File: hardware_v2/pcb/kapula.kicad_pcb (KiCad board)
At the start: 4 copper layers, 50 x 59 mm, 166 parts, among them J1 Conn_02x10_Odd_Even, J2 Conn_02x10_Odd_Even, J3 U.FL, J4 U.FL, J5 U.FL, J6 U.FL, Q1 AO3401A, Q2 AO3400A, Q3 AO3400A, Q4 AO3400A, Q5 AO3401A, Q6 BSS84, T1 BW21S7511A01TF, T2 BW21S7511A01TF, T3 BW21S7511A01TF, T4 BW21S7511A01TF, U1 TP4054, U2 DW01+G, U3 XC6206P332MR, U4 FM8002A, U5 EFR32FG14P233F256GM48-B, U6 DSB221SDN, U7 XA213-G4J, Y1 32768 Hz

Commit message: PCB: Fix TCXO model in schematic
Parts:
- U6: value DSB221SDN -> TG2016SMN 38.4000M-MCGNNM3
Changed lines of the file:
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@@
         (effects (font (size 0.7 0.7) (thickness 0.15)))
     )
-    (fp_text value "DSB221SDN" (at 0 1 90 unlocked) (layer "F.Fab")
+    (fp_text value "TG2016SMN 38.4000M-MCGNNM3" (at 0 1 90 unlocked) (layer "F.Fab")
         (effects (font (size 1 1) (thickness 0.15)))
     )

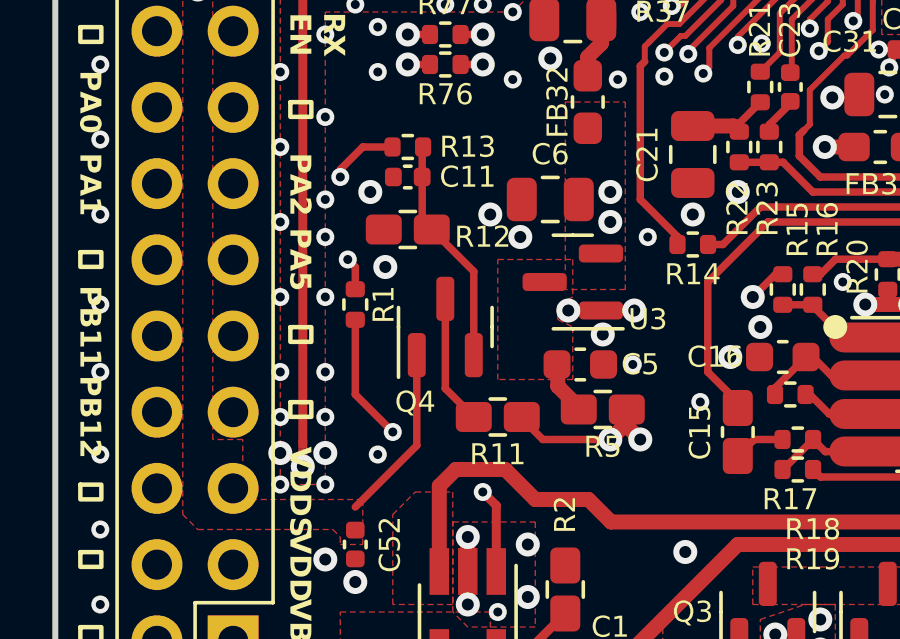
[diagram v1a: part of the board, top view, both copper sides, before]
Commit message: PCB: Add DVDD to expansion header
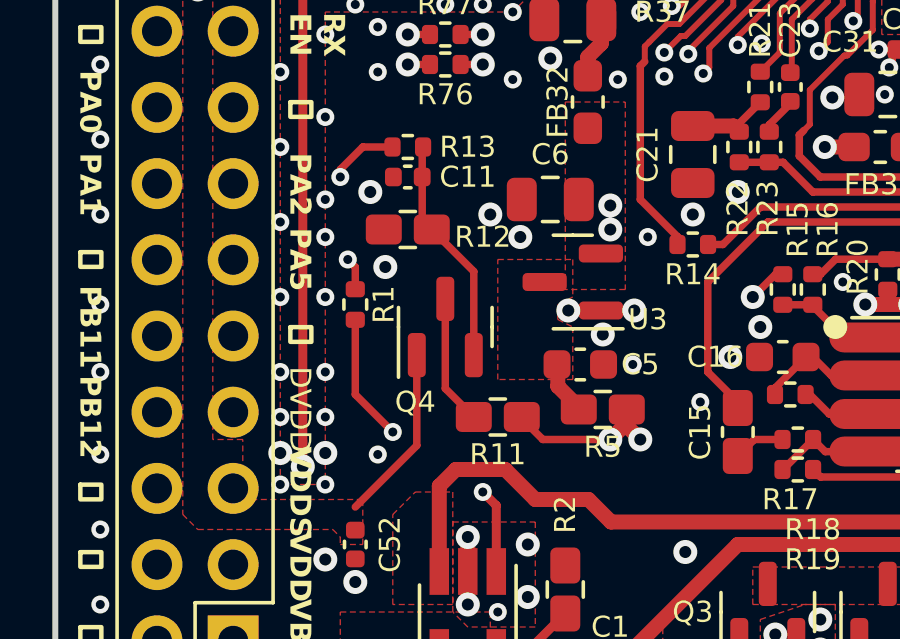
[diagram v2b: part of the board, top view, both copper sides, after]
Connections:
- J2 pad 7: GND -> /1V8
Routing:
- net /1V8: track 30.5 -> 65.0 mm
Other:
- board text added: "DVDD"

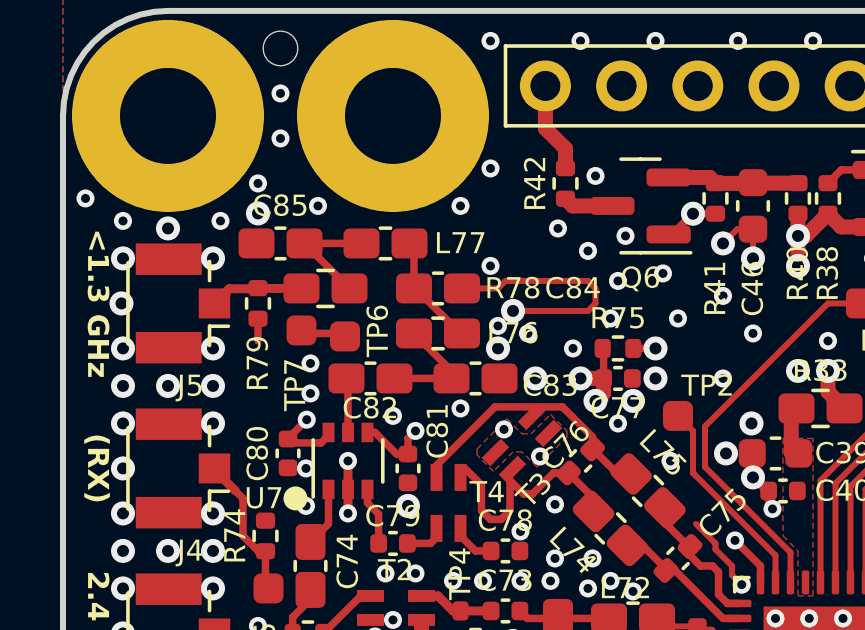
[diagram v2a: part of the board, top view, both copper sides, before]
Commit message: PCB: Optimize lowpass filter
* Reduce second harmonic stub length by 1 mm
  to move notch frequency closer to 870 MHz.
* Use footprints of correct size for capacitors and inductors.
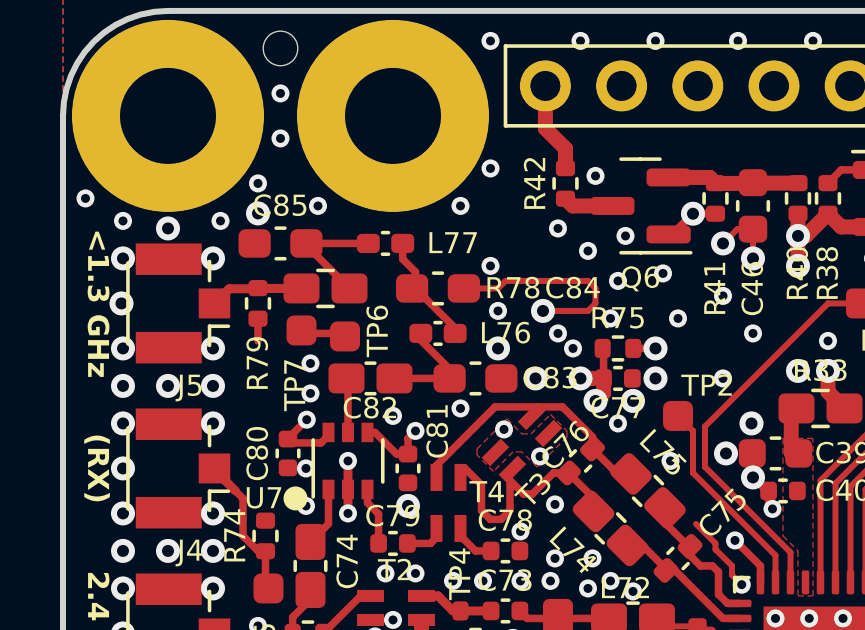
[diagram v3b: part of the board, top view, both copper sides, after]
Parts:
- C83, C84, C85: footprint kapula:C_0402_to_0603_HandSolder -> Capacitor_SMD:C_0603_1608Metric_Pad1.08x0.95mm_HandSolder
- L76, L77: footprint kapula:L_0402_to_0603_HandSolder -> Inductor_SMD:L_0402_1005Metric_Pad0.77x0.64mm_HandSolder
- moved NT72 1.00 mm to (116.5, 67.5)
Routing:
- net Net-(C84-Pad2): track 7.31 -> 6.31 mm

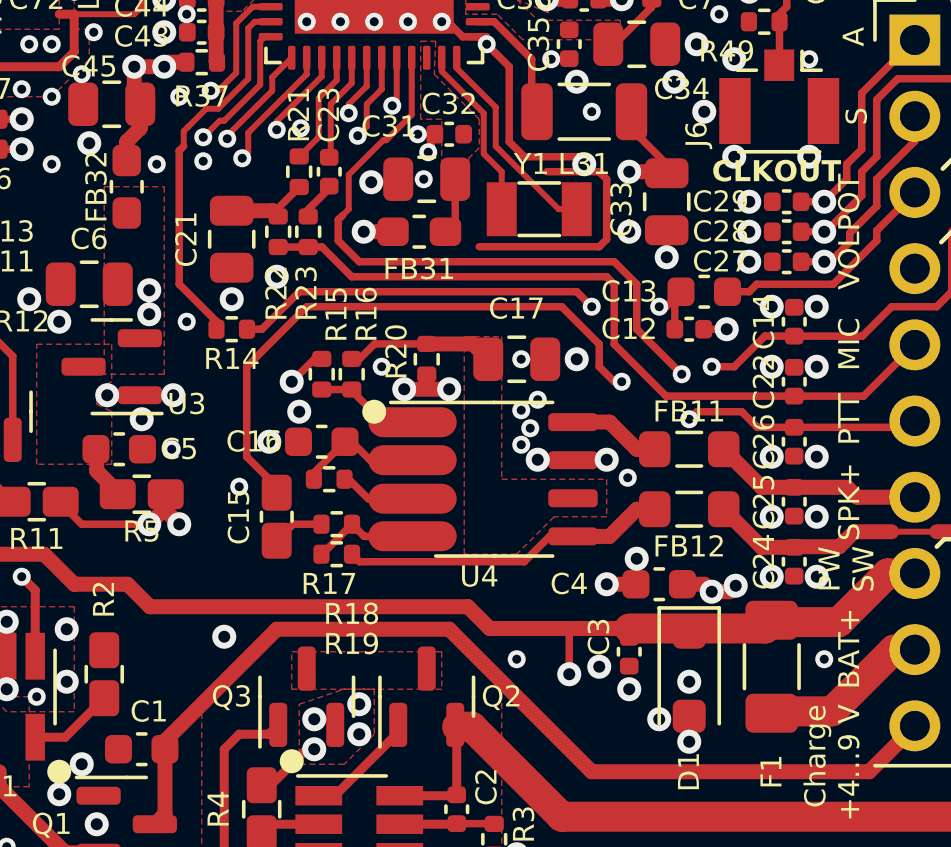
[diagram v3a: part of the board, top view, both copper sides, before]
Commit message: PCB: Changes to audio power amplifier circuit
* Increase maximum gain
* Change some footprint sizes
* Reduce shutdown pull-up resistor value
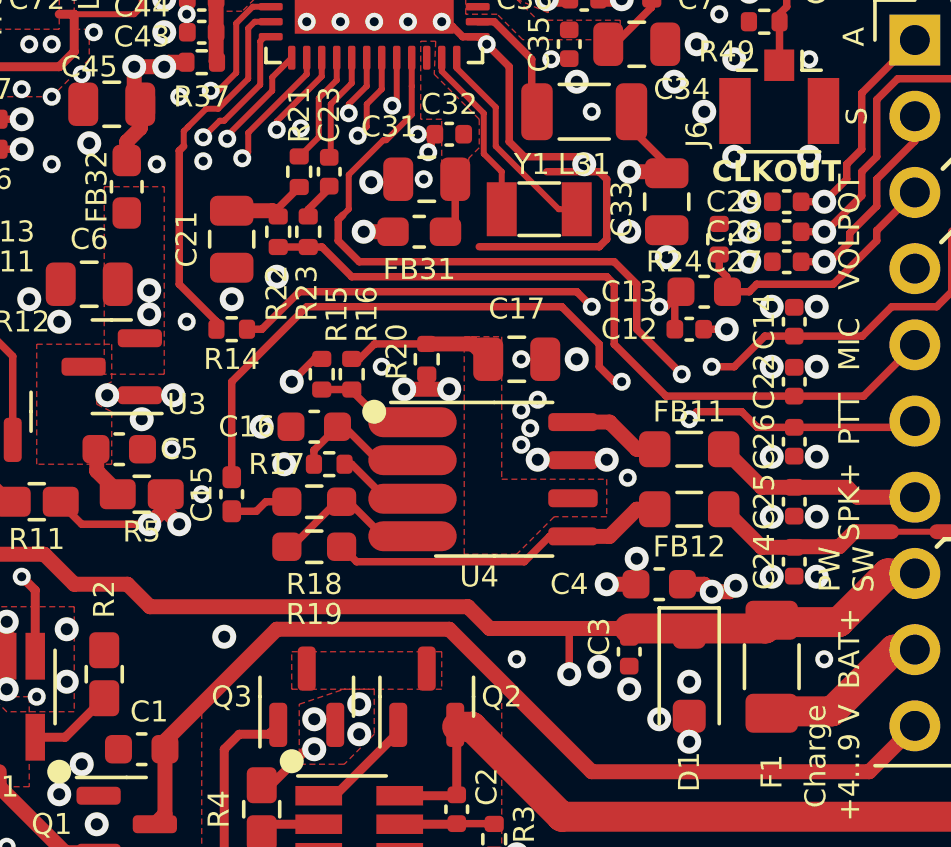
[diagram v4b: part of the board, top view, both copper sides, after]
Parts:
- added R24: 1M, Resistor_SMD:R_0402_1005Metric, F.Cu at (137.5, 89.5)
- C15: footprint kapula:C_0402_to_0603_HandSolder -> Capacitor_SMD:C_0402_1005Metric_Pad0.74x0.62mm_HandSolder
- R16: value 1M -> 330k
- R18: footprint Resistor_SMD:R_0402_1005Metric -> Resistor_SMD:R_0603_1608Metric_Pad0.98x0.95mm_HandSolder
- R19: value 22k -> 47k; footprint Resistor_SMD:R_0402_1005Metric -> Resistor_SMD:R_0603_1608Metric_Pad0.98x0.95mm_HandSolder
- moved C15 1.68 mm to (121.2, 98.0)
- moved R18 1.06 mm to (124.0, 98.2)
- moved R19 0.79 mm to (124.0, 99.8)
- moved C16 0.56 mm to (124.0, 95.8)
- moved R17 0.50 mm to (124.5, 97.0)
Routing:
- net /VOL_Out: track 7.82 -> 9.17 mm
- net /AMP+IN: track 3.51 -> 4.79 mm
- net /VOL_In: track 36.1 -> 35.1 mm
- net /AMP-IN: track 5.67 -> 6.26 mm

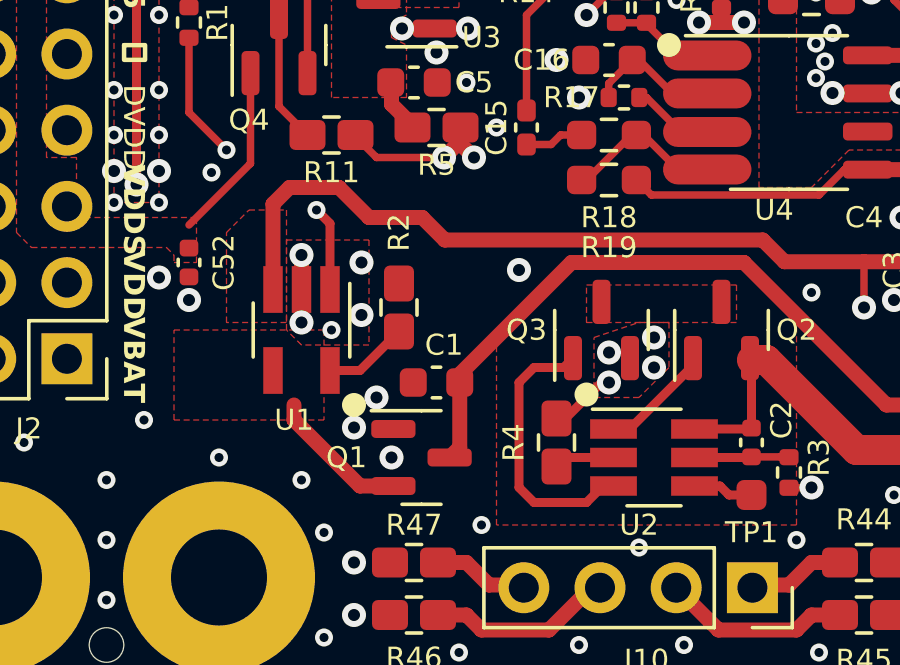
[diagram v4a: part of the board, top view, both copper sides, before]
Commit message: PCB: Improve battery charger cooling by adding zones for all pins
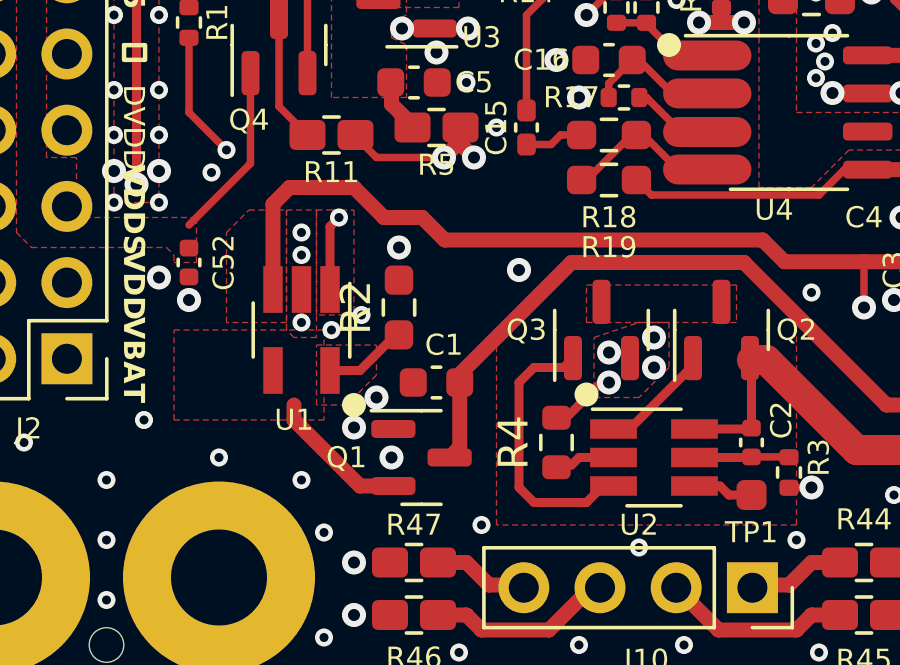
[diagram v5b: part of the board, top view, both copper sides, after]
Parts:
- R2: footprint kapula:R_0402_to_0603_HandSolder -> Resistor_SMD:R_0603_1608Metric_Pad0.98x0.95mm_HandSolder
- R4: footprint kapula:R_0402_to_0603_HandSolder -> Resistor_SMD:R_0603_1608Metric
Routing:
- net GND: track 65.4 -> 64.3 mm, vias 392 -> 393
- net /~{CHRG}: track 10.9 -> 11.5 mm
- added copper zone on F.Cu, net /BC_PROG
- added copper zone on F.Cu, net /~{CHRG}

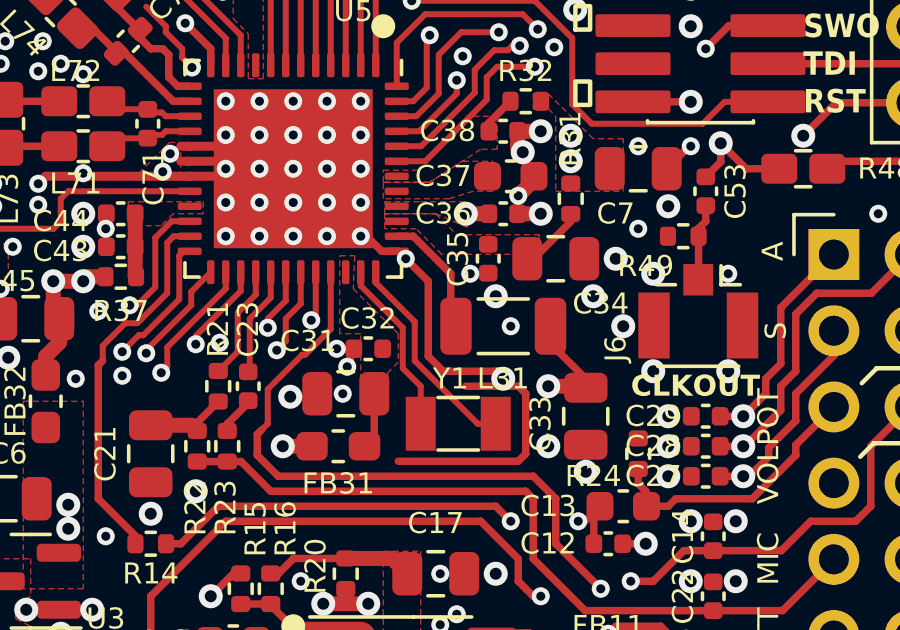
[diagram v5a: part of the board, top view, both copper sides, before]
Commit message: PCB: Move a via that was very close to EFR32 pad
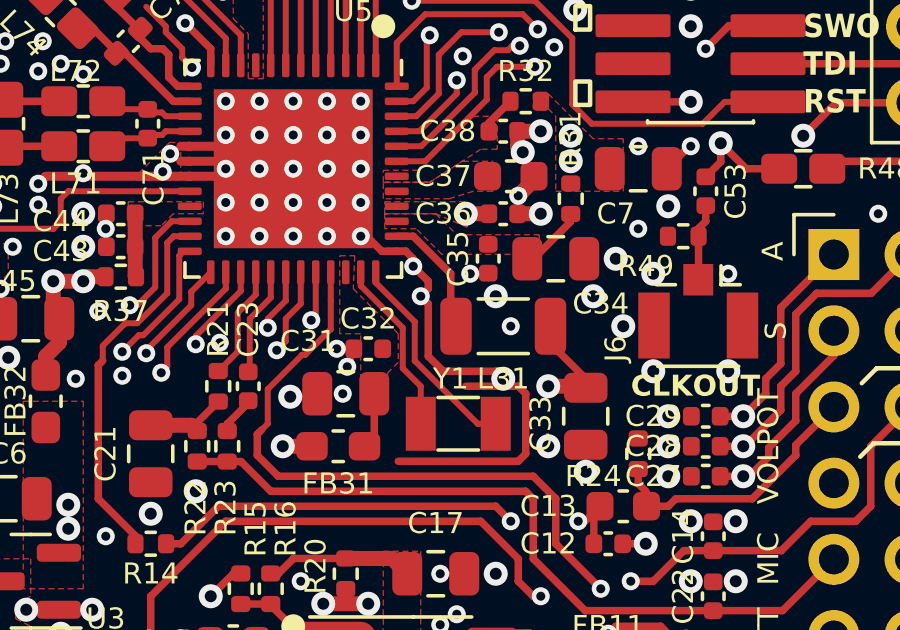
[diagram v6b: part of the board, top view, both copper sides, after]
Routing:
- net GND: track 64.3 -> 64.7 mm, vias 393 -> 394
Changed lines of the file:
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@@
   (segment (start 129.45 82.75) (end 128.95 82.75) (width 0.25) (layer "F.Cu") (net 2))
   (segment (start 128.399999 82.399999) (end 128 82) (width 0.25) (layer "F.Cu") (net 2))
+  (segment (start 130.25 84.25) (end 130.5 84.5) (width 0.25) (layer "F.Cu") (net 2))
+  (segment (start 130 83.25) (end 130.5 83.75) (width 0.25) (layer "F.Cu") (net 2))
   (segment (start 143 66.74) (end 142.51 66.74) (width 0.25) (layer "F.Cu") (net 2))
-  (segment (start 133 87) (end 132.75 86.75) (width 0.25) (layer "F.Cu") (net 2))
+  (segment (start 131 86.75) (end 132.75 86.75) (width 0.25) (layer "F.Cu") (net 2))
   (segment (start 133.5 87.25) (end 133.75 87.5) (width 0.25) (layer "F.Cu") (net 2))
+  (segment (start 129.75 82.75) (end 129.45 82.75) (width 0.25) (layer "F.Cu") (net 2))
   (segment (start 133.48 81.5) (end 134.25 81.5) (width 0.5) (layer "F.Cu") (net 2))
   (segment (start 121.75 75.45) (end 121.75 75.25) (width 0.2) (layer "F.Cu") (net 2))
@@
   (segment (start 117.750008 80.249992) (end 117.5 80.5) (width 0.3) (layer "F.Cu") (net 2))
   (segment (start 122.475 64.775) (end 122 65.25) (width 0.2) (layer "F.Cu") (net 2))
-  (segment (start 130.5 86.25) (end 130.5 83.75) (width 0.25) (layer "F.Cu") (net 2))
   (segment (start 133.5 80.9) (end 134.025 80.375) (width 0.5) (layer "F.Cu") (net 2))
-  (segment (start 131 86.75) (end 130.5 86.25) (width 0.25) (layer "F.Cu") (net 2))
-  (segment (start 129.5 82.75) (end 129.75 83) (width 0.25) (layer "F.Cu") (net 2))
+  (segment (start 130.5 84) (end 130.25 84.25) (width 0.25) (layer "F.Cu") (net 2))
   (segment (start 122.3 76.3) (end 122.3 76) (width 0.2) (layer "F.Cu") (net 2))
   (segment (start 123.75 106.5) (end 124 106.5) (width 0.3) (layer "F.Cu") (net 2))
+  (segment (start 130 83) (end 129.75 82.75) (width 0.25) (layer "F.Cu") (net 2))
   (segment (start 122.625 76.625) (end 122.5 76.5) (width 0.25) (layer "F.Cu") (net 2))
   (segment (start 121.75 75.25) (end 121.1 74.6) (width 0.2) (layer "F.Cu") (net 2))
   (segment (start 139 68.68) (end 139 69.25) (width 0.25) (layer "F.Cu") (net 2))
+  (segment (start 130.5 86.25) (end 131 86.75) (width 0.25) (layer "F.Cu") (net 2))
   (segment (start 139.2 79.25) (end 138.45 80) (width 0.25) (layer "F.Cu") (net 2))
   (segment (start 133.48 78.75) (end 134.25 78.75) (width 0.5) (layer "F.Cu") (net 2))
@@
   (segment (start 123.52 73.5) (end 123.52 73.97) (width 0.25) (layer "F.Cu") (net 2))
   (segment (start 122.625 76.625) (end 122.3 76.3) (width 0.2) (layer "F.Cu") (net 2))
+  (segment (start 130.5 84.5) (end 130.5 86.25) (width 0.25) (layer "F.Cu") (net 2))
+  (segment (start 130 83.25) (end 130 83) (width 0.25) (layer "F.Cu") (net 2))
   (segment (start 122.55 79.75) (end 122.25 79.75) (width 0.3) (layer "F.Cu") (net 2))
   (segment (start 109.5 73.45) (end 109.5 72.5) (width 0.3) (layer "F.Cu") (net 2))
-  (segment (start 132.75 86.75) (end 131 86.75) (width 0.25) (layer "F.Cu") (net 2))
   (segment (start 133.65 79.45) (end 133.48 79.28) (width 0.5) (layer "F.Cu") (net 2))
   (segment (start 142.51 66.74) (end 142.25 67) (width 0.25) (layer "F.Cu") (net 2))
@@
   (segment (start 127.45 86) (end 128.02 86) (width 0.25) (layer "F.Cu") (net 2))
   (segment (start 127.9 86.5) (end 127.8 86.6) (width 0.25) (layer "F.Cu") (net 2))
+  (segment (start 132.75 86.75) (end 133 87) (width 0.25) (layer "F.Cu") (net 2))
   (segment (start 122.25 107.7) (end 122.55 107.7) (width 0.3) (layer "F.Cu") (net 2))
   (segment (start 136.98 92.5) (end 137.75 92.5) (width 0.25) (layer "F.Cu") (net 2))
@@
   (segment (start 133.48 79.28) (end 133.48 78.75) (width 0.5) (layer "F.Cu") (net 2))
   (segment (start 134.025 80.375) (end 134.025 80.25) (width 0.5) (layer "F.Cu") (net 2))
-  (segment (start 129.45 82.75) (end 129.5 82.75) (width 0.25) (layer "F.Cu") (net 2))
   (segment (start 106.5 67.76) (end 106.5 68.5) (width 0.25) (layer "F.Cu") (net 2))
-  (segment (start 130.5 83.75) (end 129.75 83) (width 0.25) (layer "F.Cu") (net 2))
+  (segment (start 130.5 83.75) (end 130.5 84) (width 0.25) (layer "F.Cu") (net 2))
   (segment (start 133.75 89.5) (end 133.5 89.75) (width 0.25) (layer "F.Cu") (net 2))
   (segment (start 114.26 78.5) (end 115 78.5) (width 0.5) (layer "F.Cu") (net 2))
@@
   (via (at 141 103.5) (size 0.6) (drill 0.3) (layers "F.Cu" "B.Cu") (free) (net 2))
   (via (at 113 76.5) (size 0.6) (drill 0.3) (layers "F.Cu" "B.Cu") (free) (net 2))
+  (via (at 130.25 84.25) (size 0.6) (drill 0.3) (layers "F.Cu" "B.Cu") (net 2))
   (via (at 124 105.5) (size 0.8) (drill 0.4) (layers "F.Cu" "B.Cu") (free) (net 2))
   (via (at 114.25 84.5) (size 0.6) (drill 0.3) (layers "F.Cu" "B.Cu") (free) (net 2))
@@
   (via (at 107.25 113.75) (size 0.6) (drill 0.3) (layers "F.Cu" "B.Cu") (free) (net 2))
   (via (at 143 66) (size 0.6) (drill 0.3) (layers "F.Cu" "B.Cu") (free) (net 2))
-  (via (at 129.75 83) (size 0.6) (drill 0.3) (layers "F.Cu" "B.Cu") (net 2))
+  (via (at 130 83.25) (size 0.6) (drill 0.3) (layers "F.Cu" "B.Cu") (net 2))
   (via (at 141.25 63.75) (size 0.6) (drill 0.3) (layers "F.Cu" "B.Cu") (free) (net 2))
   (via (at 141 69.25) (size 0.6) (drill 0.3) (layers "F.Cu" "B.Cu") (free) (net 2))
